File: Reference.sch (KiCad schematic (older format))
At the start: 6 parts, among them IC601 MAX6126AASA25+

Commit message: name change on main for sheets
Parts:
- renumbered C605 to C?, C603 to C?, C601 to C?, C602 to C?, C604 to C?, IC601 to IC?
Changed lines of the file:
@@
 $EndDescr
 $Comp
-L MAX6126AASA25+:MAX6126AASA25+ IC601
+L MAX6126AASA25+:MAX6126AASA25+ IC?
 U 1 1 60C8EC90
 P 5800 4000
-F 0 "IC601" H 6350 4265 50  0000 C CNN
+F 0 "IC?" H 6350 4265 50  0000 C CNN
 F 1 "MAX6126AASA25+" H 6350 4174 50  0000 C CNN
 F 2 "footprint libraries:MAX6126-25+" H 6750 4100 50  0001 L CNN
@@
 REFERENCE_2.5V
 $Comp
-L Device:C C605
+L Device:C C?
 U 1 1 60C8FD88
 P 7050 4350
-F 0 "C605" H 7165 4396 50  0000 L CNN
+F 0 "C?" H 7165 4396 50  0000 L CNN
 F 1 "0.1u" H 7165 4305 50  0000 L CNN
 F 2 "Capacitor_SMD:C_0402_1005Metric" H 7088 4200 50  0001 C CNN
@@
 $EndComp
 $Comp
-L power:GND #PWR0605
+L power:GND #PWR?
 U 1 1 60C90CD5
 P 7050 4500
-F 0 "#PWR0605" H 7050 4250 50  0001 C CNN
+F 0 "#PWR?" H 7050 4250 50  0001 C CNN
 F 1 "GND" H 7055 4327 50  0000 C CNN
 F 2 "" H 7050 4500 50  0001 C CNN
@@
 	5650 3650 5450 3650
 $Comp
-L Device:C C603
+L Device:C C?
 U 1 1 60C92A79
 P 5450 3800
-F 0 "C603" H 5335 3846 50  0000 R CNN
+F 0 "C?" H 5335 3846 50  0000 R CNN
 F 1 "0.1u" H 5335 3755 50  0000 R CNN
 F 2 "Capacitor_SMD:C_0402_1005Metric" H 5488 3650 50  0001 C CNN
@@
 $EndComp
 $Comp
-L power:GND #PWR0603
+L power:GND #PWR?
 U 1 1 60C940A0
 P 5450 3950
-F 0 "#PWR0603" H 5450 3700 50  0001 C CNN
+F 0 "#PWR?" H 5450 3700 50  0001 C CNN
 F 1 "GND" H 5300 3900 50  0000 C CNN
 F 2 "" H 5450 3950 50  0001 C CNN
@@
 Connection ~ 5750 4300
 $Comp
-L power:GND #PWR0601
+L power:GND #PWR?
 U 1 1 60C94E50
 P 4850 4400
-F 0 "#PWR0601" H 4850 4150 50  0001 C CNN
+F 0 "#PWR?" H 4850 4150 50  0001 C CNN
 F 1 "GND" H 4855 4227 50  0000 C CNN
 F 2 "" H 4850 4400 50  0001 C CNN
@@
 $EndComp
 $Comp
-L power:GND #PWR0604
+L power:GND #PWR?
 U 1 1 60C9528F
 P 5750 4600
-F 0 "#PWR0604" H 5750 4350 50  0001 C CNN
+F 0 "#PWR?" H 5750 4350 50  0001 C CNN
 F 1 "GND" H 5755 4427 50  0000 C CNN
 F 2 "" H 5750 4600 50  0001 C CNN
@@
 $EndComp
 $Comp
-L Device:C C601
+L Device:C C?
 U 1 1 60C96AC6
 P 4850 4250
-F 0 "C601" H 4735 4296 50  0000 R CNN
+F 0 "C?" H 4735 4296 50  0000 R CNN
 F 1 "0.1u" H 4735 4205 50  0000 R CNN
 F 2 "Capacitor_SMD:C_0402_1005Metric" H 4888 4100 50  0001 C CNN
@@
 	5400 4100 4850 4100
 $Comp
-L Device:C C602
+L Device:C C?
 U 1 1 60D5F3BC
 P 5250 4350
-F 0 "C602" H 5100 4400 50  0000 R CNN
+F 0 "C?" H 5100 4400 50  0000 R CNN
 F 1 "0.1u" H 5150 4300 50  0000 R CNN
 F 2 "Capacitor_SMD:C_0402_1005Metric" H 5288 4200 50  0001 C CNN
@@
 $EndComp
 $Comp
-L Device:C C604
+L Device:C C?
 U 1 1 60D605F7
 P 5550 4350
-F 0 "C604" H 5450 4400 50  0000 R CNN
+F 0 "C?" H 5450 4400 50  0000 R CNN
 F 1 "1u" H 5450 4300 50  0000 R CNN
 F 2 "Capacitor_SMD:C_0402_1005Metric" H 5588 4200 50  0001 C CNN

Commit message: redo annotations
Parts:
- gave numbers to parts that had none: 6
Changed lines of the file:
@@
 $EndDescr
 $Comp
-L MAX6126AASA25+:MAX6126AASA25+ IC?
+L MAX6126AASA25+:MAX6126AASA25+ IC701
 U 1 1 60C8EC90
 P 5800 4000
-F 0 "IC?" H 6350 4265 50  0000 C CNN
+F 0 "IC701" H 6350 4265 50  0000 C CNN
 F 1 "MAX6126AASA25+" H 6350 4174 50  0000 C CNN
 F 2 "footprint libraries:MAX6126-25+" H 6750 4100 50  0001 L CNN
@@
 REFERENCE_2.5V
 $Comp
-L Device:C C?
+L Device:C C705
 U 1 1 60C8FD88
 P 7050 4350
-F 0 "C?" H 7165 4396 50  0000 L CNN
+F 0 "C705" H 7165 4396 50  0000 L CNN
 F 1 "0.1u" H 7165 4305 50  0000 L CNN
 F 2 "Capacitor_SMD:C_0402_1005Metric" H 7088 4200 50  0001 C CNN
@@
 $EndComp
 $Comp
-L power:GND #PWR?
+L power:GND #PWR0704
 U 1 1 60C90CD5
 P 7050 4500
-F 0 "#PWR?" H 7050 4250 50  0001 C CNN
+F 0 "#PWR0704" H 7050 4250 50  0001 C CNN
 F 1 "GND" H 7055 4327 50  0000 C CNN
 F 2 "" H 7050 4500 50  0001 C CNN
@@
 	5650 3650 5450 3650
 $Comp
-L Device:C C?
+L Device:C C703
 U 1 1 60C92A79
 P 5450 3800
-F 0 "C?" H 5335 3846 50  0000 R CNN
+F 0 "C703" H 5335 3846 50  0000 R CNN
 F 1 "0.1u" H 5335 3755 50  0000 R CNN
 F 2 "Capacitor_SMD:C_0402_1005Metric" H 5488 3650 50  0001 C CNN
@@
 $EndComp
 $Comp
-L power:GND #PWR?
+L power:GND #PWR0702
 U 1 1 60C940A0
 P 5450 3950
-F 0 "#PWR?" H 5450 3700 50  0001 C CNN
+F 0 "#PWR0702" H 5450 3700 50  0001 C CNN
 F 1 "GND" H 5300 3900 50  0000 C CNN
 F 2 "" H 5450 3950 50  0001 C CNN
@@
 Connection ~ 5750 4300
 $Comp
-L power:GND #PWR?
+L power:GND #PWR0701
 U 1 1 60C94E50
 P 4850 4400
-F 0 "#PWR?" H 4850 4150 50  0001 C CNN
+F 0 "#PWR0701" H 4850 4150 50  0001 C CNN
 F 1 "GND" H 4855 4227 50  0000 C CNN
 F 2 "" H 4850 4400 50  0001 C CNN
@@
 $EndComp
 $Comp
-L power:GND #PWR?
+L power:GND #PWR0703
 U 1 1 60C9528F
 P 5750 4600
-F 0 "#PWR?" H 5750 4350 50  0001 C CNN
+F 0 "#PWR0703" H 5750 4350 50  0001 C CNN
 F 1 "GND" H 5755 4427 50  0000 C CNN
 F 2 "" H 5750 4600 50  0001 C CNN
@@
 $EndComp
 $Comp
-L Device:C C?
+L Device:C C701
 U 1 1 60C96AC6
 P 4850 4250
-F 0 "C?" H 4735 4296 50  0000 R CNN
+F 0 "C701" H 4735 4296 50  0000 R CNN
 F 1 "0.1u" H 4735 4205 50  0000 R CNN
 F 2 "Capacitor_SMD:C_0402_1005Metric" H 4888 4100 50  0001 C CNN
@@
 	5400 4100 4850 4100
 $Comp
-L Device:C C?
+L Device:C C702
 U 1 1 60D5F3BC
 P 5250 4350
-F 0 "C?" H 5100 4400 50  0000 R CNN
+F 0 "C702" H 5100 4400 50  0000 R CNN
 F 1 "0.1u" H 5150 4300 50  0000 R CNN
 F 2 "Capacitor_SMD:C_0402_1005Metric" H 5288 4200 50  0001 C CNN
@@
 $EndComp
 $Comp
-L Device:C C?
+L Device:C C704
 U 1 1 60D605F7
 P 5550 4350
-F 0 "C?" H 5450 4400 50  0000 R CNN
+F 0 "C704" H 5450 4400 50  0000 R CNN
 F 1 "1u" H 5450 4300 50  0000 R CNN
 F 2 "Capacitor_SMD:C_0402_1005Metric" H 5588 4200 50  0001 C CNN

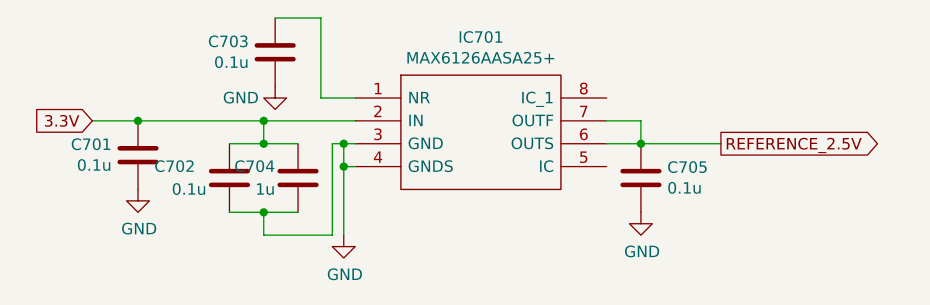
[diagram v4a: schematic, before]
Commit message: finished everything. notes: thick traces, gnd pours, keep outs/pwr plane, DRC Errors
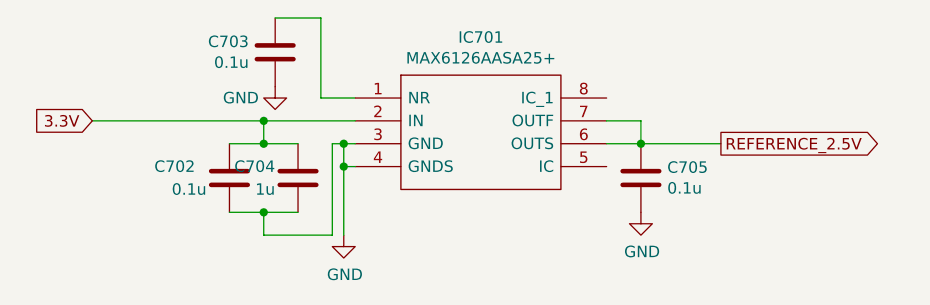
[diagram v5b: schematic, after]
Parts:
- removed C701: 0.1u, Capacitor_SMD:C_0402_1005Metric, symbol Device:C
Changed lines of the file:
@@
 Connection ~ 5750 4300
-$Comp
-L power:GND #PWR0701
-U 1 1 60C94E50
-P 4850 4400
-F 0 "#PWR0701" H 4850 4150 50  0001 C CNN
-F 1 "GND" H 4855 4227 50  0000 C CNN
-F 2 "" H 4850 4400 50  0001 C CNN
-F 3 "" H 4850 4400 50  0001 C CNN
-	1    4850 4400
-	1    0    0    -1
-$EndComp
 $Comp
 L power:GND #PWR0703
@@
 	1    0    0    -1
 $EndComp
-$Comp
-L Device:C C701
-U 1 1 60C96AC6
-P 4850 4250
-F 0 "C701" H 4735 4296 50  0000 R CNN
-F 1 "0.1u" H 4735 4205 50  0000 R CNN
-F 2 "Capacitor_SMD:C_0402_1005Metric" H 4888 4100 50  0001 C CNN
-F 3 "~" H 4850 4250 50  0001 C CNN
-	1    4850 4250
-	1    0    0    -1
-$EndComp
-Wire Wire Line
-	4850 4100 4650 4100
-Connection ~ 4850 4100
 Wire Wire Line
 	5400 4100 5400 4200
 Connection ~ 5400 4100
-Wire Wire Line
-	5400 4100 4850 4100
 $Comp
 L Device:C C702
@@
 	5700 4200 5750 4200
 Connection ~ 5750 4200
+Wire Wire Line
+	4650 4100 5400 4100
 $EndSCHEMATC
